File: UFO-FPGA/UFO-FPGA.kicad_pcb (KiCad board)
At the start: 4 copper layers, 68.6 x 53.3 mm, 109 parts, among them J1 Power, J2 Digital, J3 Digital/PWM, J4 Digital, J5 USB_B_Micro, J6 Conn_02x02_Counter_Clockwise, Q1 2N7002, U1 ICE40HX8K-BG121, U2 FT2232HL, U3 ASDMB-12MHz, U5 93LC56CT-I/MS, U6 PWR convert, U7 PWR convert, U9 N25Q032A13ESC40F

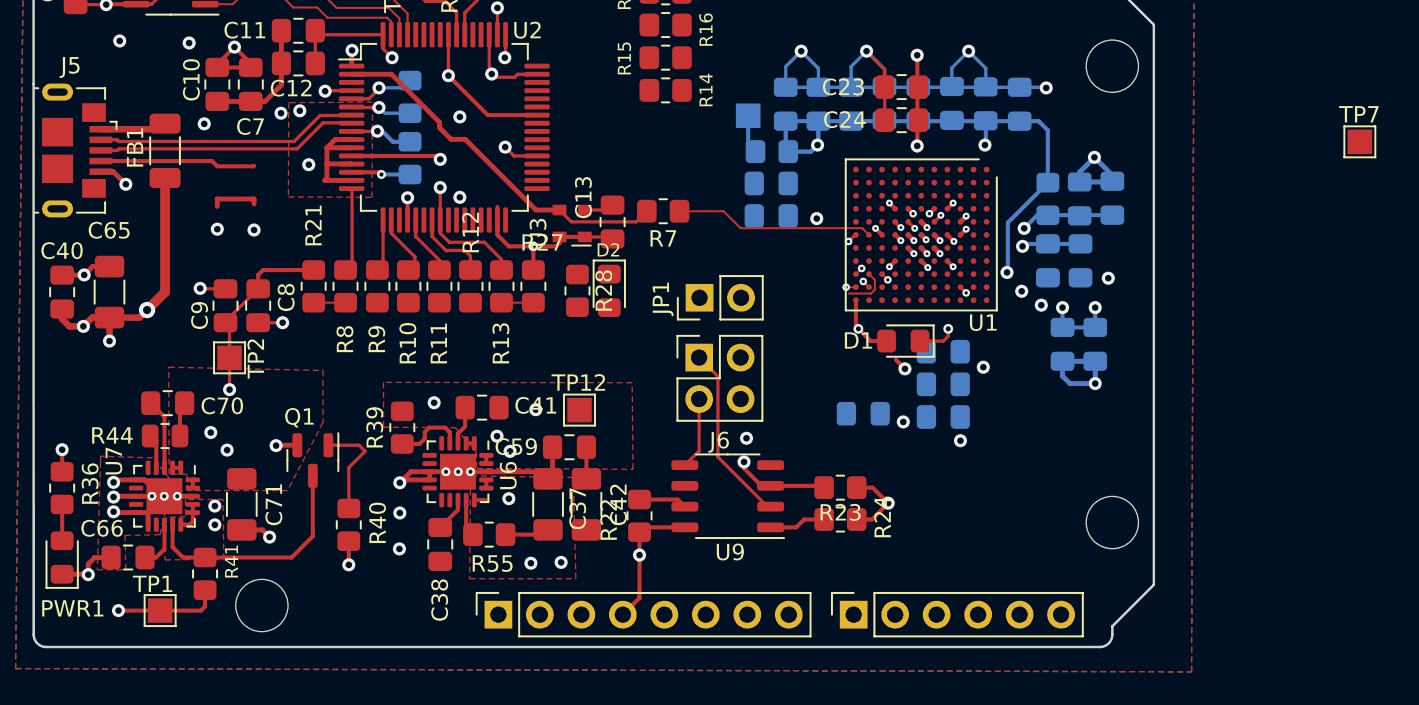
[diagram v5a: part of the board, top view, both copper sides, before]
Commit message: PCB placement
spi connected
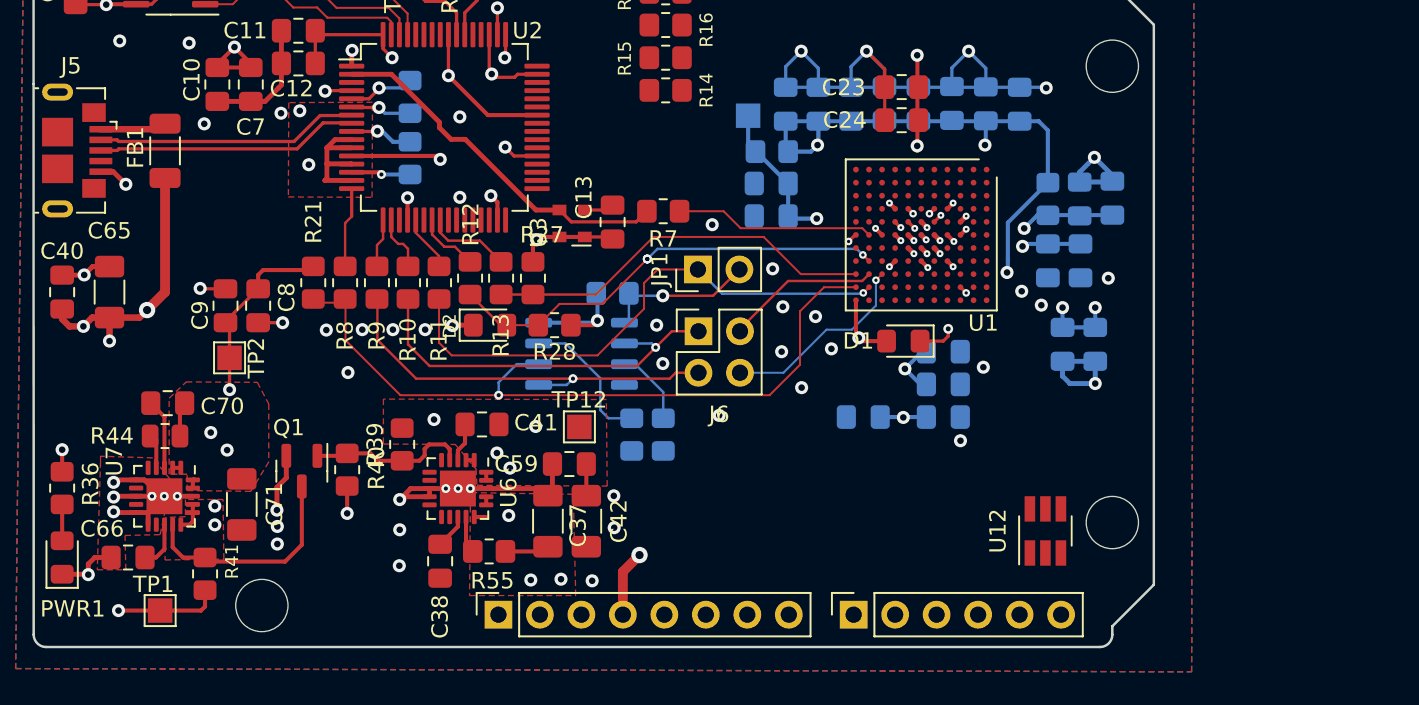
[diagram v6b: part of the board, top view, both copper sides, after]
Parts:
- removed TP7: TestPoint, TestPoint:TestPoint_Pad_1.5x1.5mm
- added U12: MAX11116AUT+T, Package_TO_SOT_SMD:SOT-23-6_Handsoldering, F.Cu at (173.4, 94.4)
- R22, R23, R24, U9: moved to B.Cu
- moved R24 19.7 mm to (146.9, 79.8), turned to 0 degrees
- moved U9 12.5 mm to (145.1, 83.5)
- moved R23 11.3 mm to (150.1, 88.5), turned to 90 degrees
- moved D2 7.60 mm to (139.4, 81.8), turned to 0 degrees
- moved R22 5.00 mm to (148.1, 88.5)
- moved R40 3.38 mm to (130.7, 90.6)
- moved R28 2.52 mm to (143.4, 81.8), turned to 180 degrees
- moved JP1 1.74 mm to (152.2, 78.4)
- moved J6 1.61 mm to (152.2, 82.2)
- moved C37 1.03 mm to (143.0, 93.8)
- moved C42 1.03 mm to (145.3, 93.8)
- moved C59 1.03 mm to (144.3, 90.3)
- moved R55 1.03 mm to (139.4, 95.6)
- moved TP12 1.03 mm to (144.9, 88.0)
- moved R39 1.03 mm to (134.1, 89.1)
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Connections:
- J6 pad 2: /BANK 4 - SPI Programming/ICE_MOSI -> /BANK 4 - SPI Programming/ICE_MISO
- J6 pad 4: /BANK 4 - SPI Programming/ICE_MISO -> /BANK 4 - SPI Programming/ICE_MOSI
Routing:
- net ICE_SCK: track 2.74 -> 45.2 mm
- net ICE_SS_B: track 0.49 -> 33.2 mm
- net ICE_CDONE: track 0.00 -> 28.1 mm, vias 0 -> 3
- net ICE_CREST: track 2.44 -> 24.1 mm, vias 1 -> 0
- net Flash-MOSI: track 4.41 -> 25.3 mm, vias 0 -> 1
- net Flash-MISO: track 10.9 -> 24.0 mm, vias 0 -> 1
- net /BANK 4 - SPI Programming/ICE_MOSI: track 0.49 -> 12.1 mm
- net unconnected-(J5-ID-Pad4): track 9.58 -> 0.00 mm
- net /BANK 4 - SPI Programming/ICE_MISO: track 2.80 -> 9.43 mm
- net /BANK 4 - SPI Programming/VCCPLL0: track 2.32 -> 8.94 mm
- net /BANK 4 - SPI Programming/N25-CS: track 3.47 -> 9.41 mm, vias 0 -> 1
- net /BANK 4 - SPI Programming/N25-HOLD: track 2.96 -> 8.74 mm
- net /USB Programmer/ICE-CREST: track 7.86 -> 5.24 mm, vias 1 -> 0
- net GND: track 142.0 -> 140.7 mm, vias 60 -> 77
- net /BANK 4 - SPI Programming/N25-WP: track 5.79 -> 4.68 mm, vias 1 -> 0
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
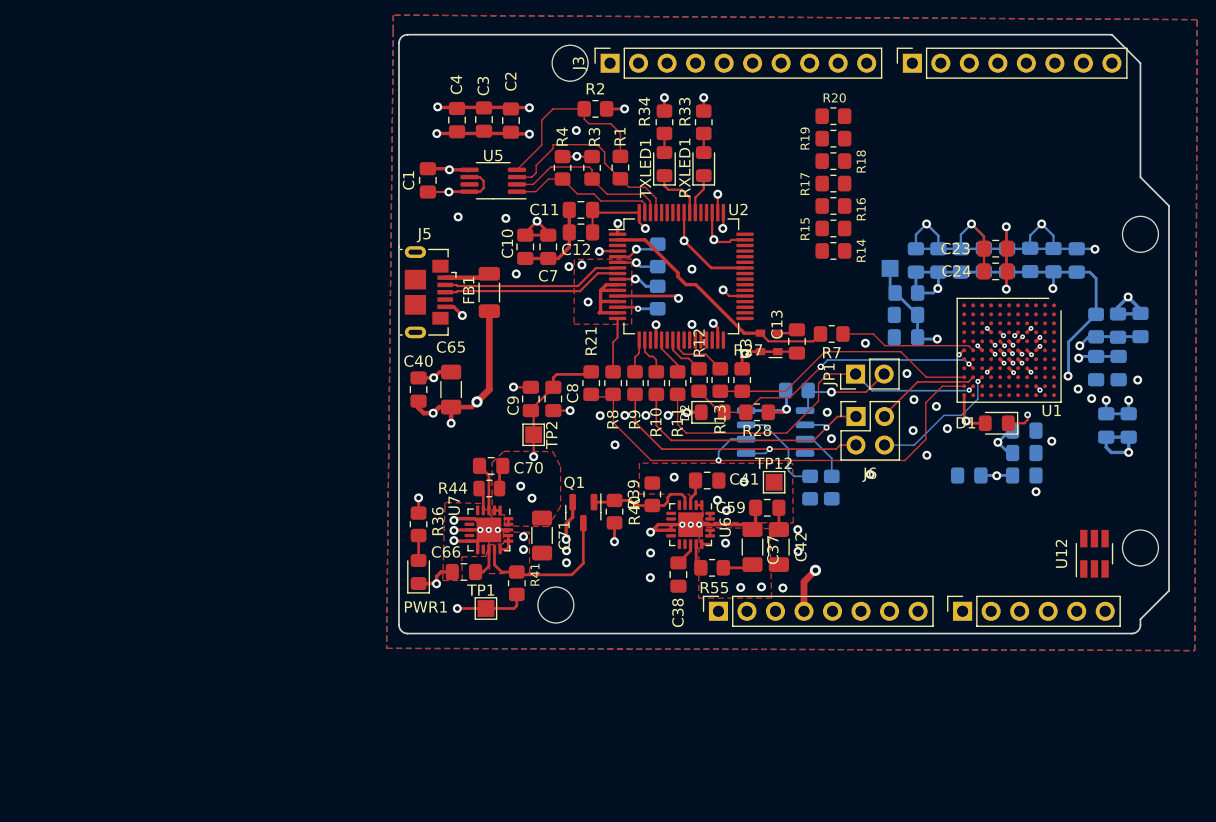
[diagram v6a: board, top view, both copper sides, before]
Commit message: pcb 0603
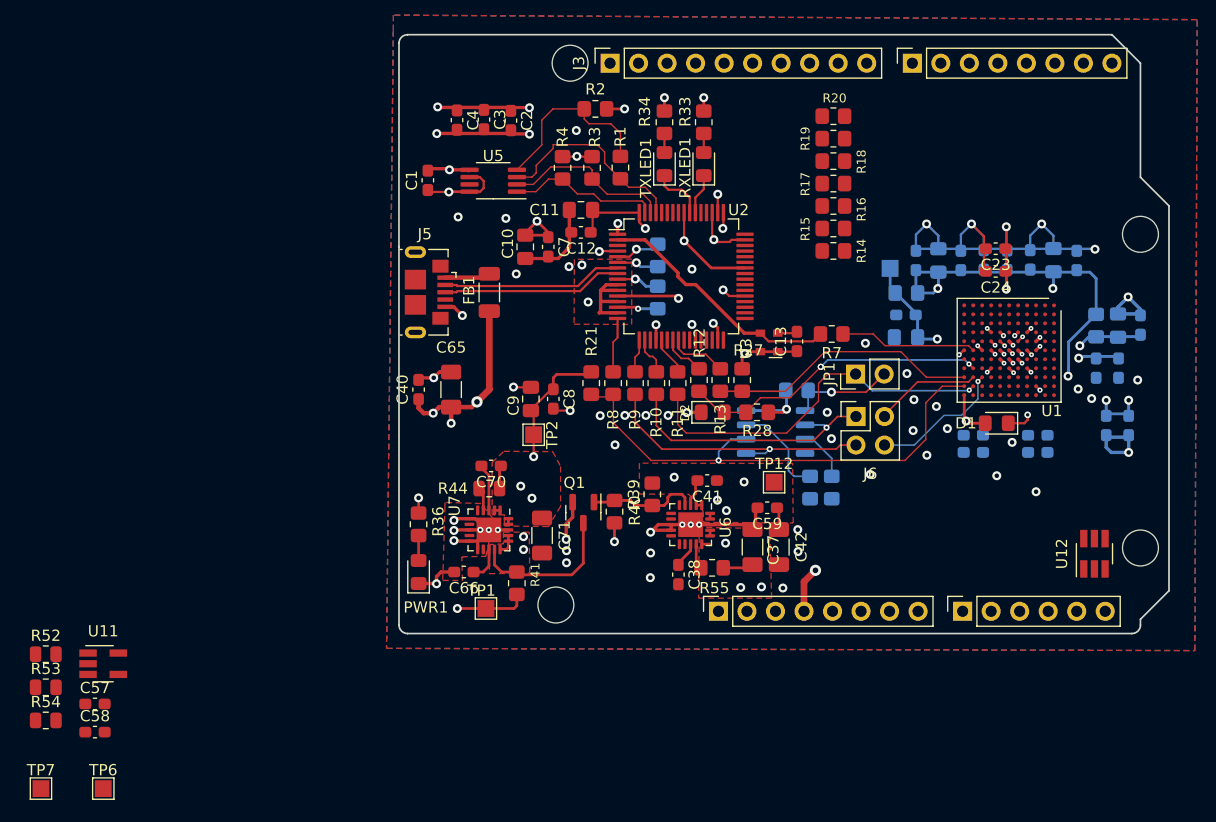
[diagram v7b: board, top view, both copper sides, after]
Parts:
- added C57: 100pF, Capacitor_SMD:C_0603_1608Metric_Pad1.08x0.95mm_HandSolder, F.Cu at (84.4, 107.8)
- added C58: 100pF, Capacitor_SMD:C_0603_1608Metric_Pad1.08x0.95mm_HandSolder, F.Cu at (84.4, 110.3)
- added R52: 510, Resistor_SMD:R_0805_2012Metric, F.Cu at (80.0, 103.3)
- added R53: 510, Resistor_SMD:R_0805_2012Metric, F.Cu at (80.0, 106.3)
- added R54: 10, Resistor_SMD:R_0805_2012Metric, F.Cu at (80.0, 109.2)
- added TP6: TestPoint, TestPoint:TestPoint_Pad_1.5x1.5mm, F.Cu at (85.2, 115.3)
- added TP7: TestPoint, TestPoint:TestPoint_Pad_1.5x1.5mm, F.Cu at (79.6, 115.3)
- added U11: TL071, Package_TO_SOT_SMD:SOT-23-5_HandSoldering, F.Cu at (85.2, 104.2)
- C1, C12, C13, C15, C16, C17, C2, C20, C21, C22, C23, C24, C29, C3, C30, C31, C32, C38, C4, C40, C41, C59, C60, C61, C62, C64, C66, C67, C69, C7, C70, C8: footprint Capacitor_SMD:C_0805_2012Metric_Pad1.18x1.45mm_HandSolder -> Capacitor_SMD:C_0603_1608Metric_Pad1.08x0.95mm_HandSolder
- moved C29 5.78 mm to (162.7, 83.8), turned to 180 degrees
- moved C30 2.09 mm to (162.7, 85.3)
- moved C22 1.27 mm to (168.4, 83.8)
- moved C21 1.20 mm to (168.4, 85.3)
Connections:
- J2 pad 6: AIN1_O -> AIN1
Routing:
- net +3V3: track 113.7 -> 107.4 mm
- net GND: vias 77 -> 76

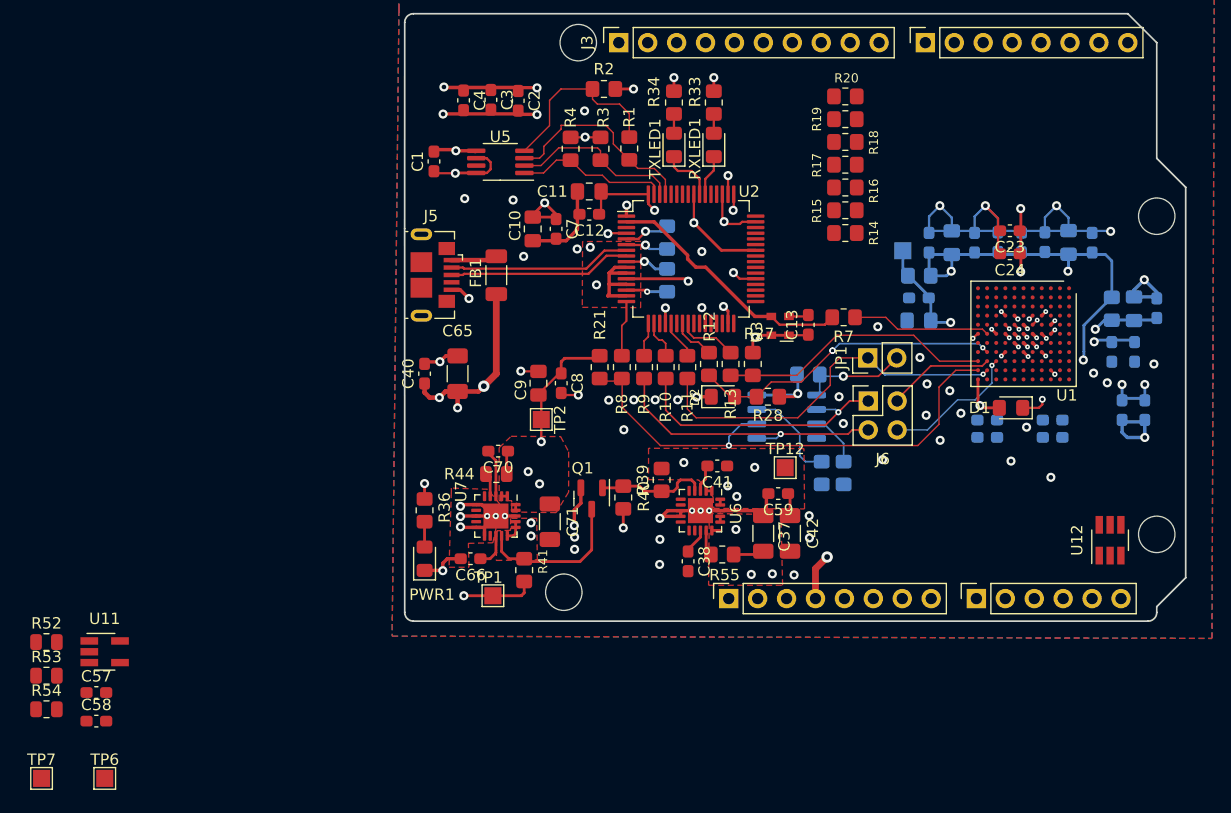
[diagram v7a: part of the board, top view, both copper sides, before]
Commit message: pcb and footprints
0603
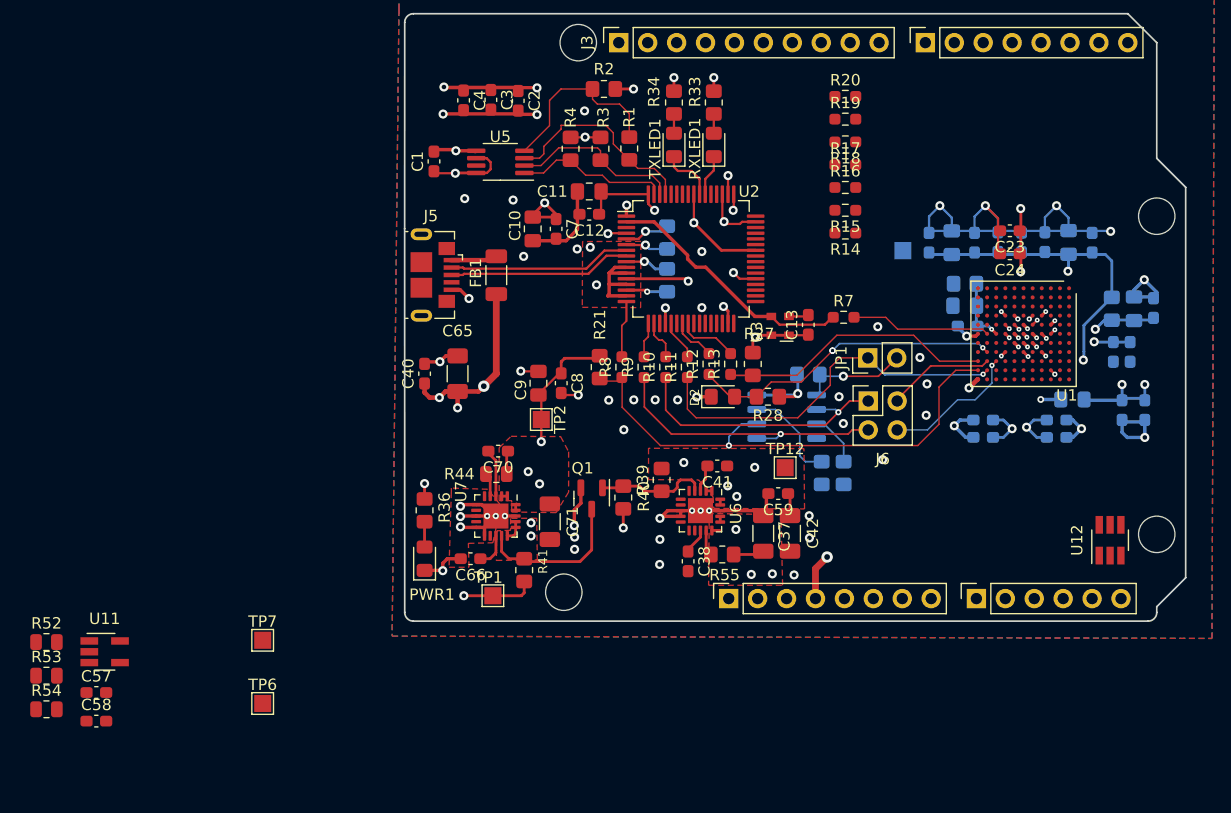
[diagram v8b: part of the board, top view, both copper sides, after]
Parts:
- D1: moved to B.Cu
- R10, R11, R12, R13, R14, R15, R16, R17, R18, R19, R20, R7, R8, R9: footprint Resistor_SMD:R_0805_2012Metric_Pad1.20x1.40mm_HandSolder -> Resistor_SMD:R_0603_1608Metric_Pad0.98x0.95mm_HandSolder
- moved TP7 22.9 mm to (99.0, 103.2)
- moved TP6 15.3 mm to (99.0, 108.7)
- moved D1 5.45 mm to (170.1, 82.0), turned to 0 degrees
- moved C17 4.93 mm to (160.9, 75.6)
- moved C18 4.23 mm to (160.7, 73.8)
- moved R25 4.07 mm to (160.7, 71.9), turned to 180 degrees
- moved C32 0.39 mm to (175.2, 77.8)
- moved C21 0.35 mm to (168.8, 85.3)
- moved C22 0.35 mm to (168.8, 83.8)
- moved C29 0.35 mm to (162.3, 83.8)
- moved C30 0.35 mm to (162.3, 85.3)
- moved C20 0.28 mm to (177.3, 74.0)
- moved C31 0.14 mm to (173.7, 77.8)
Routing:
- net GND: track 140.7 -> 149.6 mm, vias 76 -> 71
- net +3V3: track 107.4 -> 115.4 mm
- net +1V2: track 37.6 -> 32.4 mm, vias 11 -> 10
- net /BANK 4 - SPI Programming/VCCPLL0: track 8.94 -> 5.68 mm, vias 2 -> 1
- net +2V5: track 2.79 -> 2.28 mm
